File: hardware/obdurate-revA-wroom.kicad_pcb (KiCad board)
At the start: 4 copper layers, 40 x 40 mm, 46 parts, among them J2 USB-C receptacle, Q1 P-ch MOSFET, U1 SN65HVD230DR, U2 LM5164-Q1, U3 ESP32-S3-WROOM-1-N8R8, U4 AP2112K-3.3

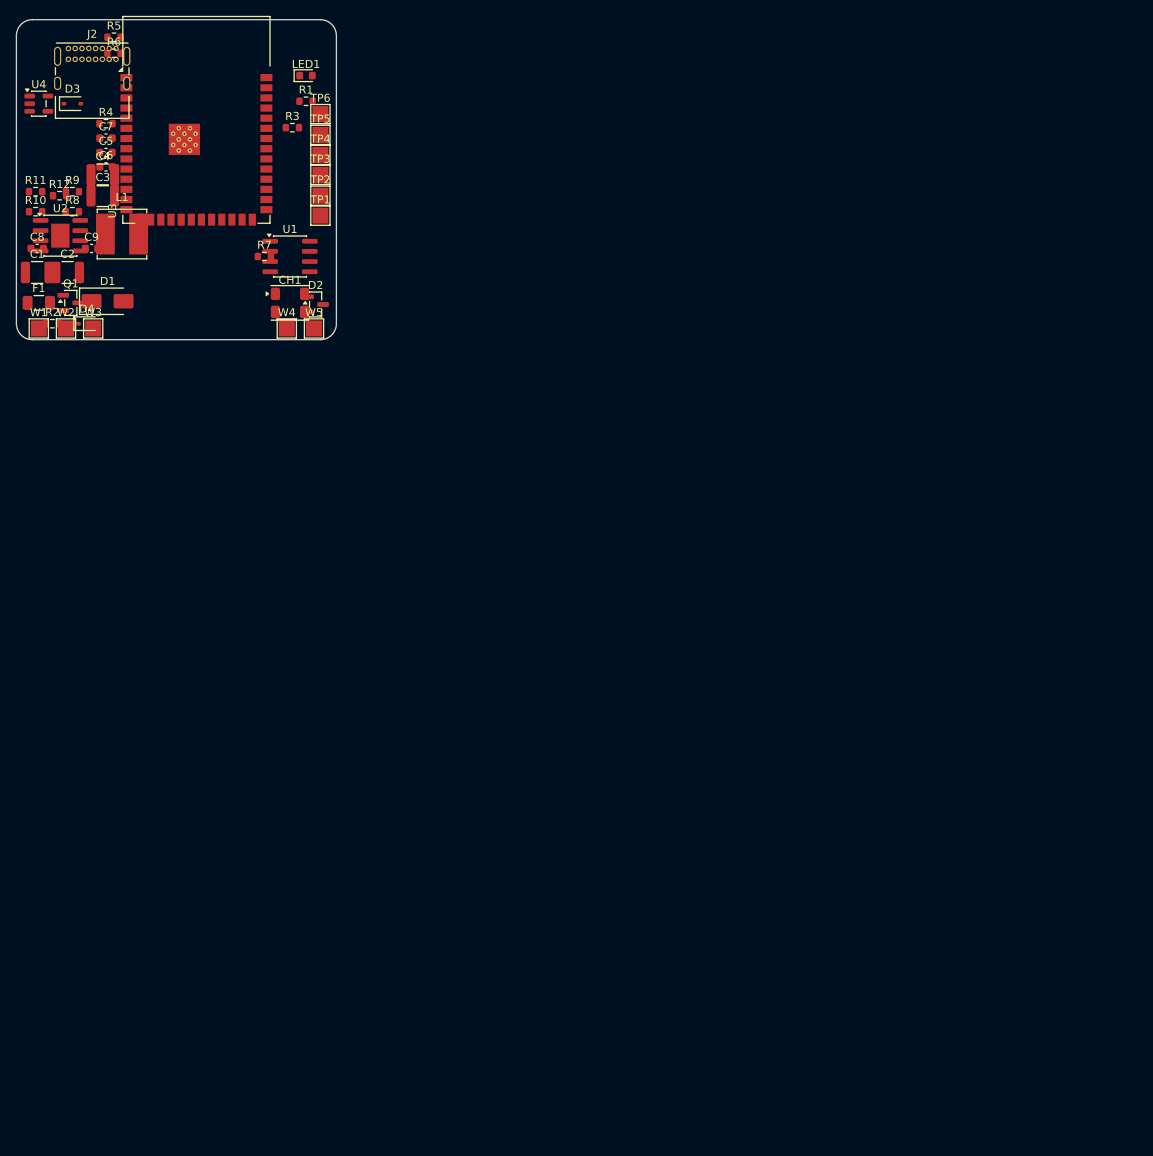
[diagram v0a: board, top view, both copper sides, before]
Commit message: Quote the board, and let three real vendors correct it
Two days of talking to fabs, and the design is better for it. Every change here
came from a vendor saying no to something.

TWO LAYERS, not four. LionCircuits price 4-layer at roughly four times 2-layer,
and this board does not need it: nothing on the xiao carrier is fast - CAN runs
at 500 kbit over 9 mm, the USB is on the module, there is no memory bus - and the
placement already clusters the power stage so the switching loop stays tight. GND
becomes a filled pour on B.Cu instead of a buried plane. build_board.py now takes
the layer count as a parameter, so "xiao:2 wroom:4" builds both from one set of
CSVs rather than forking the design. The wroom variant stays at 4 layers because
it carries the USB pair and a PCB antenna.

GND is now an actual pour. Both inner layers previously shipped as empty artwork,
which is a legitimate DFM failure on a 4-layer order.

REAL PART NUMBERS throughout, because nothing can be auto-quoted from
"2.2 uF 100 V X7R". Choosing actual parts found a real error: D4 was a 15 V zener
clamping the gate of an AO3401A, which is rated +-12 V Vgs - the clamp would have
exceeded the rating it exists to protect. It is a 10 V zener now.

C1/C2 drop from 2.2 uF to 1 uF, both at 100 V. 2.2 uF at 100 V in 1210 is a
specialty size that BOTH vendors failed to identify; 1 uF 100 V is commodity. Two
of them give 2 uF, which the LM5164 will not notice. The 100 V rating stays - it
is for load-dump survival, not capacitance precision.

Corrected a claim of mine that today disproved: bom.csv said the LM5164 was
likely long-lead in India and should be consigned. LionCircuits quoted it in
stock at INR 539. A stale warning in a BOM is worse than no warning.

THREE VENDOR EXPORTERS, one per house, because the same 26 components need three
incompatible files and I got all three wrong by inferring before reading:

  make_assembly_bom.py   LionCircuits - one row per designator, Item and
                         D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
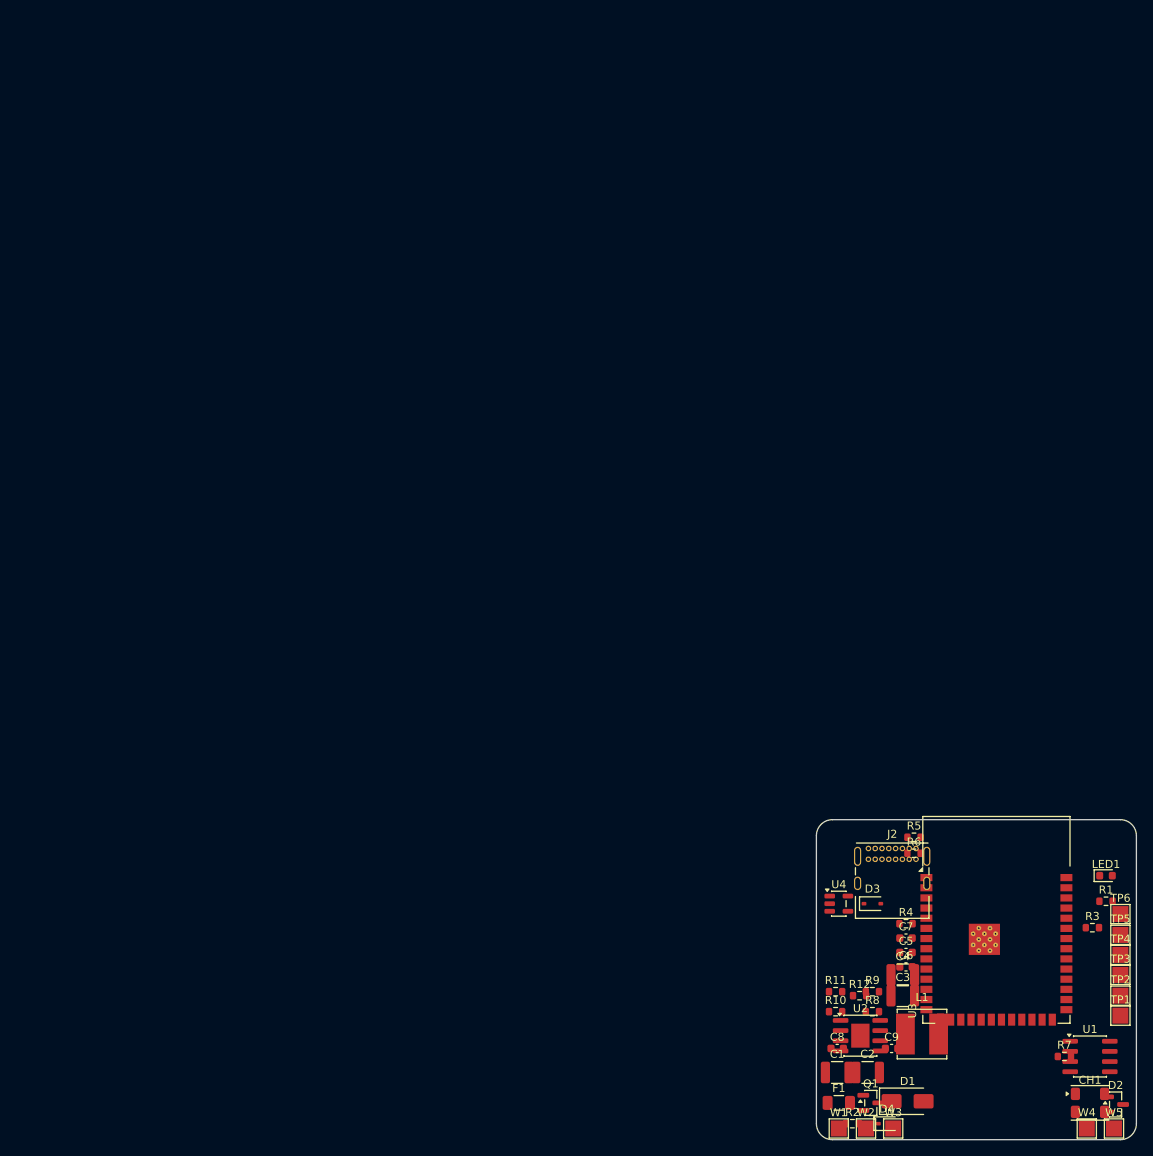
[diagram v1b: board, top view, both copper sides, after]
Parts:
- moved C1 141.4 mm to (82.6, 111.6)
- moved C2 141.4 mm to (86.4, 111.6)
- moved C3 141.4 mm to (90.8, 102.0)
- moved C4 141.4 mm to (90.8, 99.4)
- moved C5 141.4 mm to (91.2, 96.6)
- moved C6 141.4 mm to (91.2, 98.4)
- moved C7 141.4 mm to (91.2, 94.8)
- moved C8 141.4 mm to (82.6, 108.6)
- moved C9 141.4 mm to (89.4, 108.6)
- moved CH1 141.4 mm to (114.2, 115.4)
- moved D1 141.4 mm to (91.4, 115.2)
- moved D2 141.4 mm to (117.4, 115.6)
- moved D3 141.4 mm to (87.0, 90.5)
- moved D4 141.4 mm to (88.8, 118.0)
- moved F1 141.4 mm to (82.8, 115.4)
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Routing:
- added copper zone on In1.Cu, net GND
- added copper zone on In2.Cu, net GND
